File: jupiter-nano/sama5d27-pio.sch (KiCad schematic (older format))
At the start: 2 parts, among them U1 ATSAMA5D27C-LD1G-CU

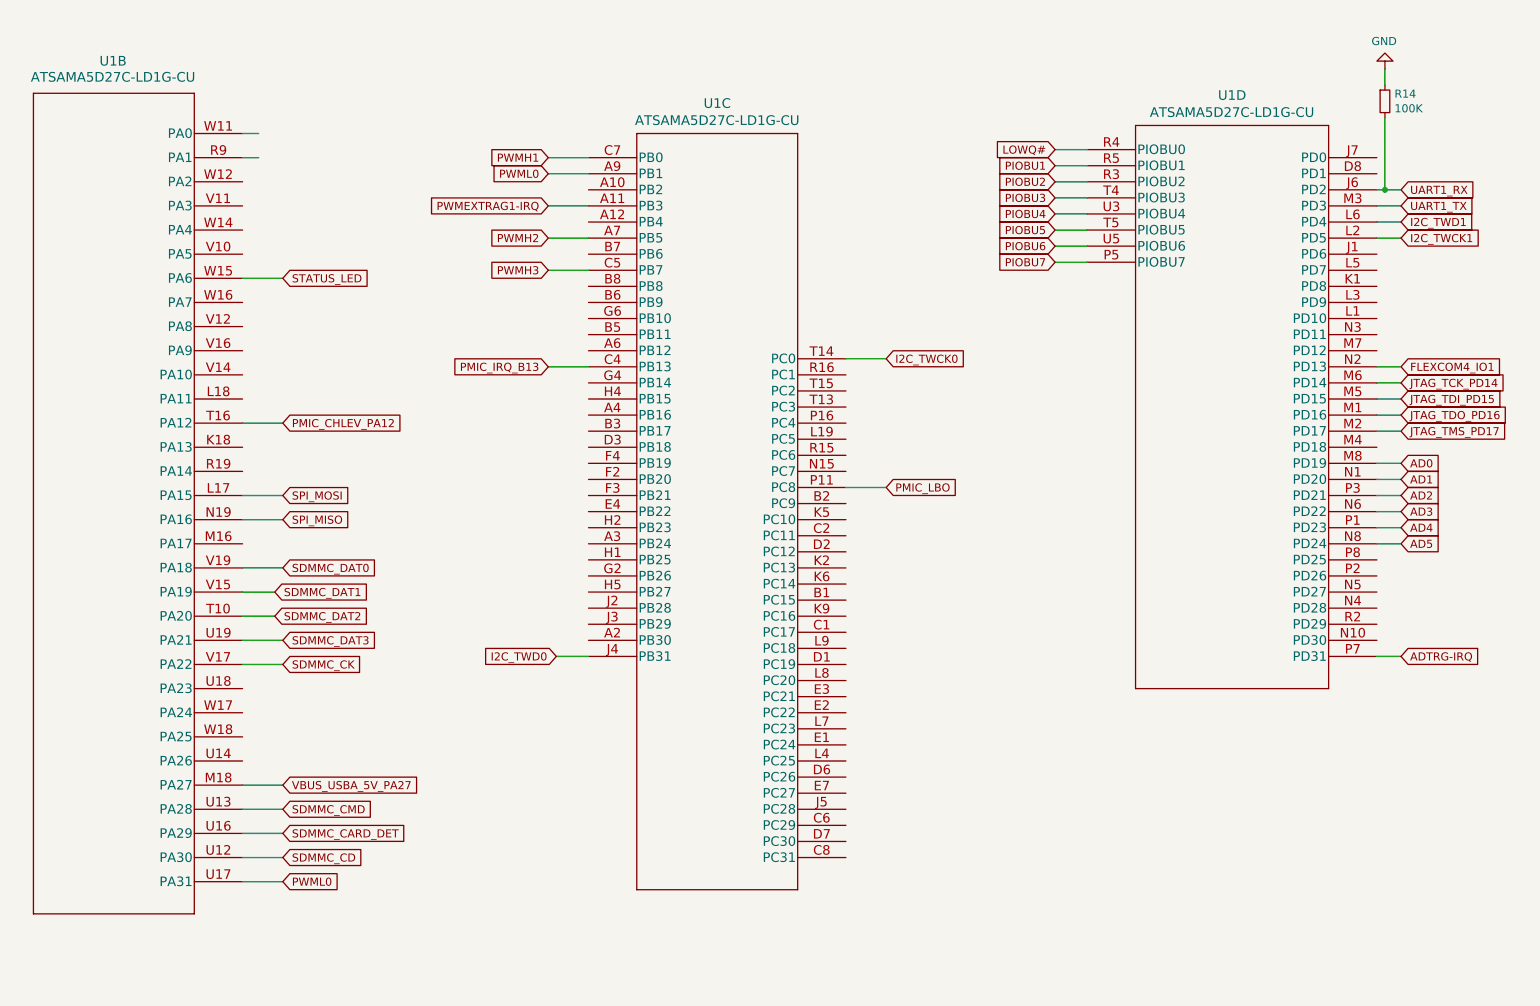
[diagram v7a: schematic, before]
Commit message: numerous ERC fixes
- still more to go
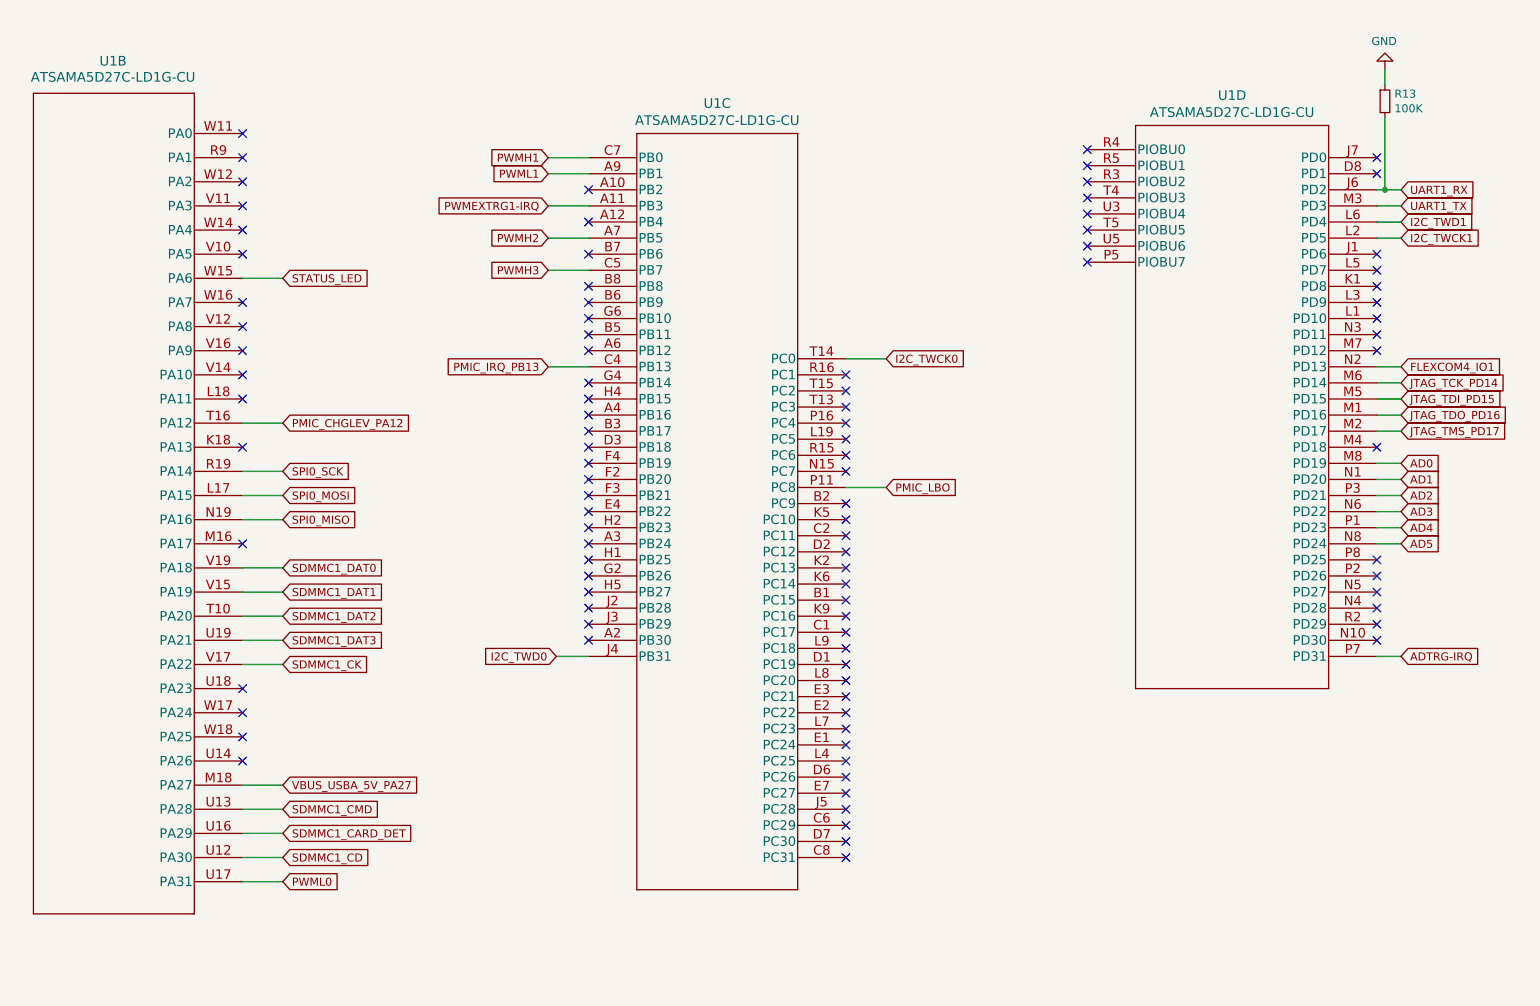
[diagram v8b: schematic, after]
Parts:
- renumbered R14 to R13
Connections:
- net PWML0: no longer U1.A9 (PB1)
- net SPI0_SCK: now reaches U1.R19 (PA14)
- net LOWQ#: no longer names the net of U1.R4 (PIOBU0)
- net PIOBU1: no longer names the net of U1.R5 (PIOBU1)
- net PIOBU2: no longer names the net of U1.R3 (PIOBU2)
- net PIOBU3: no longer names the net of U1.T4 (PIOBU3)
- net PIOBU4: no longer names the net of U1.U3 (PIOBU4)
- net PIOBU5: no longer names the net of U1.T5 (PIOBU5)
- net PIOBU6: no longer names the net of U1.U5 (PIOBU6)
- net PIOBU7: no longer names the net of U1.P5 (PIOBU7)
- net PMIC_CHLEV_PA12 renamed PMIC_CHGLEV_PA12
- net PMIC_IRQ_B13 renamed PMIC_IRQ_PB13
- net PWMEXTRAG1-IRQ renamed PWMEXTRG1-IRQ
- net SDMMC_CARD_DET renamed SDMMC1_CARD_DET
- net SDMMC_CD renamed SDMMC1_CD
- net SDMMC_CK renamed SDMMC1_CK
- net SDMMC_CMD renamed SDMMC1_CMD
- net SDMMC_DAT0 renamed SDMMC1_DAT0
- net SDMMC_DAT1 renamed SDMMC1_DAT1
- net SDMMC_DAT2 renamed SDMMC1_DAT2
- net SDMMC_DAT3 renamed SDMMC1_DAT3
- net SPI_MISO renamed SPI0_MISO
- net SPI_MOSI renamed SPI0_MOSI
- new net PWML1: U1.A9 (PB1)
- no-connect marks 0 -> 96
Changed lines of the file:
@@
 	1    0    0    -1
 $EndComp
-Wire Wire Line
-	2000 2150 2250 2150
 Text GLabel 2250 2150 2    50   Input ~ 0
 STATUS_LED
 Text GLabel 2250 3050 2    50   Input ~ 0
-PMIC_CHLEV_PA12
+PMIC_CHGLEV_PA12
 Text GLabel 2250 3500 2    50   Input ~ 0
-SPI_MOSI
+SPI0_MOSI
 Text GLabel 2250 3650 2    50   Input ~ 0
-SPI_MISO
+SPI0_MISO
 Text GLabel 2250 3950 2    50   Input ~ 0
-SDMMC_DAT0
-Text GLabel 2200 4100 2    50   Input ~ 0
-SDMMC_DAT1
-Text GLabel 2200 4250 2    50   Input ~ 0
-SDMMC_DAT2
+SDMMC1_DAT0
+Text GLabel 2250 4100 2    50   Input ~ 0
+SDMMC1_DAT1
+Text GLabel 2250 4250 2    50   Input ~ 0
+SDMMC1_DAT2
 Text GLabel 2250 4400 2    50   Input ~ 0
-SDMMC_DAT3
+SDMMC1_DAT3
 Text GLabel 2250 4550 2    50   Input ~ 0
-SDMMC_CK
+SDMMC1_CK
 Text GLabel 2250 5450 2    50   Input ~ 0
-SDMMC_CMD
+SDMMC1_CMD
 Text GLabel 2250 5750 2    50   Input ~ 0
-SDMMC_CD
+SDMMC1_CD
 Text GLabel 2250 5900 2    50   Input ~ 0
 PWML0
 Text GLabel 3900 1500 0    50   Input ~ 0
-PWML0
-Wire Wire Line
-	2000 3050 2250 3050
+PWML1
 Wire Wire Line
 	2000 3500 2250 3500
@@
 $EndComp
 Wire Wire Line
-	2000 1250 2100 1250
-Wire Wire Line
-	2000 1400 2100 1400
-Wire Wire Line
 	4150 1400 3900 1400
 Wire Wire Line
@@
 	2000 3950 2250 3950
 Wire Wire Line
-	2000 4100 2200 4100
-Wire Wire Line
-	2000 4250 2200 4250
+	2000 4100 2250 4100
+Wire Wire Line
+	2000 4250 2250 4250
 Wire Wire Line
 	2000 4400 2250 4400
@@
 PWMH1
 Text GLabel 3900 1700 0    50   Input ~ 0
-PWMEXTRAG1-IRQ
+PWMEXTRG1-IRQ
 Text GLabel 3900 1900 0    50   Input ~ 0
 PWMH2
@@
 	3900 2100 4150 2100
 Text GLabel 3900 2700 0    50   Input ~ 0
-PMIC_IRQ_B13
+PMIC_IRQ_PB13
 Text GLabel 3950 4500 0    50   Input ~ 0
 I2C_TWD0
@@
 Text GLabel 6000 3450 2    50   Input ~ 0
 PMIC_LBO
-Wire Wire Line
-	7250 1350 7050 1350
-Wire Wire Line
-	7250 1450 7050 1450
-Wire Wire Line
-	7250 1550 7050 1550
-Wire Wire Line
-	7250 1650 7050 1650
-Wire Wire Line
-	7250 1750 7050 1750
-Wire Wire Line
-	7250 1850 7050 1850
-Wire Wire Line
-	7250 1950 7050 1950
-Wire Wire Line
-	7250 2050 7050 2050
-Text GLabel 7050 1350 0    50   Input ~ 0
-LOWQ#
-Text GLabel 7050 1450 0    50   Input ~ 0
-PIOBU1
-Text GLabel 7050 1550 0    50   Input ~ 0
-PIOBU2
-Text GLabel 7050 1650 0    50   Input ~ 0
-PIOBU3
-Text GLabel 7050 1750 0    50   Input ~ 0
-PIOBU4
-Text GLabel 7050 1850 0    50   Input ~ 0
-PIOBU5
-Text GLabel 7050 1950 0    50   Input ~ 0
-PIOBU6
-Text GLabel 7050 2050 0    50   Input ~ 0
-PIOBU7
 Wire Wire Line
 	9050 1600 9100 1600
@@
 ADTRG-IRQ
 $Comp
-L Device:R_Small R14
+L Device:R_Small R13
 U 1 1 600D6DFE
 P 9100 1050
-F 0 "R14" H 9159 1096 50  0000 L CNN
+F 0 "R13" H 9159 1096 50  0000 L CNN
 F 1 "100K" H 9159 1005 50  0000 L CNN
 F 2 "" H 9100 1050 50  0001 C CNN
@@
 	9100 950  9100 850
 $Comp
-L power:GND #PWR0123
+L power:GND #PWR024
 U 1 1 600DB627
 P 9100 850
-F 0 "#PWR0123" H 9100 600 50  0001 C CNN
+F 0 "#PWR024" H 9100 600 50  0001 C CNN
 F 1 "GND" H 9105 677 50  0000 C CNN
 F 2 "" H 9100 850 50  0001 C CNN
@@
 JTAG_TCK_PD14
 Text GLabel 2250 5600 2    50   Input ~ 0
-SDMMC_CARD_DET
+SDMMC1_CARD_DET
 Wire Wire Line
 	2000 5600 2250 5600
@@
 Text GLabel 2250 5300 2    50   Input ~ 0
 VBUS_USBA_5V_PA27
+NoConn ~ 2000 1250
+NoConn ~ 2000 1400
+NoConn ~ 2000 1700
+NoConn ~ 2000 1550
+NoConn ~ 2000 1850
+NoConn ~ 2000 2000
+NoConn ~ 2000 2300
+Wire Wire Line
+	2000 2150 2250 2150
+NoConn ~ 2000 2450
+NoConn ~ 2000 2600
+NoConn ~ 2000 2750
+NoConn ~ 2000 2900
+Wire Wire Line
+	2000 3050 2250 3050
+NoConn ~ 2000 3200
+NoConn ~ 2000 3800
+NoConn ~ 2000 4850
+NoConn ~ 2000 4700
+NoConn ~ 2000 5000
+NoConn ~ 2000 5150
+NoConn ~ 4150 1600
+NoConn ~ 4150 1800
+NoConn ~ 4150 2000
+NoConn ~ 4150 2200
+NoConn ~ 4150 2300
+NoConn ~ 4150 2400
+NoConn ~ 4150 2500
+NoConn ~ 4150 2600
+NoConn ~ 4150 2800
+NoConn ~ 4150 2900
+NoConn ~ 4150 3000
+NoConn ~ 4150 3100
+NoConn ~ 4150 3200
+NoConn ~ 4150 3300
+NoConn ~ 4150 3400
+NoConn ~ 4150 3500
+NoConn ~ 4150 3600
+NoConn ~ 4150 3700
+NoConn ~ 4150 3800
+NoConn ~ 4150 3900
+NoConn ~ 4150 4000
+NoConn ~ 4150 4100
+NoConn ~ 4150 4200
+NoConn ~ 4150 4300
+NoConn ~ 4150 4400
+NoConn ~ 5750 2750
+NoConn ~ 5750 2850
+NoConn ~ 5750 2950
+NoConn ~ 5750 3050
+NoConn ~ 5750 3150
+NoConn ~ 5750 3250
+NoConn ~ 5750 3350
+NoConn ~ 5750 3550
+NoConn ~ 5750 3650
+NoConn ~ 5750 3750
+NoConn ~ 5750 3850
+NoConn ~ 5750 3950
+NoConn ~ 5750 4050
+NoConn ~ 5750 4150
+NoConn ~ 5750 4250
+NoConn ~ 5750 4350
+NoConn ~ 5750 4450
+NoConn ~ 5750 4550
+NoConn ~ 5750 4650
+NoConn ~ 5750 4750
+NoConn ~ 5750 4850
+NoConn ~ 5750 4950
+NoConn ~ 5750 5050
+NoConn ~ 5750 5150
+NoConn ~ 5750 5250
+NoConn ~ 5750 5350
+NoConn ~ 5750 5450
+NoConn ~ 5750 5550
+NoConn ~ 5750 5650
+NoConn ~ 5750 5750
+NoConn ~ 9050 4400
+NoConn ~ 9050 4300
+NoConn ~ 9050 4200
+NoConn ~ 9050 4100
+NoConn ~ 9050 4000
+NoConn ~ 9050 3900
+NoConn ~ 9050 3200
+NoConn ~ 9050 2600
+NoConn ~ 9050 2500
+NoConn ~ 9050 2400
+NoConn ~ 9050 2300
+NoConn ~ 9050 1500
+NoConn ~ 9050 1400
+Text GLabel 2250 3350 2    50   Input ~ 0
+SPI0_SCK
+Wire Wire Line
+	2000 3350 2250 3350
+NoConn ~ 7250 1350
+NoConn ~ 7250 1450
+NoConn ~ 7250 1550
+NoConn ~ 7250 1650
+NoConn ~ 7250 1750
+NoConn ~ 7250 1850
+NoConn ~ 7250 1950
+NoConn ~ 7250 2050
+NoConn ~ 9050 2200
+NoConn ~ 9050 2100
+NoConn ~ 9050 2000
 $EndSCHEMATC
